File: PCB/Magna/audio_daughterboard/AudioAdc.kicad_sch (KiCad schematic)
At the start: 22 parts, among them J201 PSG01550, U201 WM8782SEDS

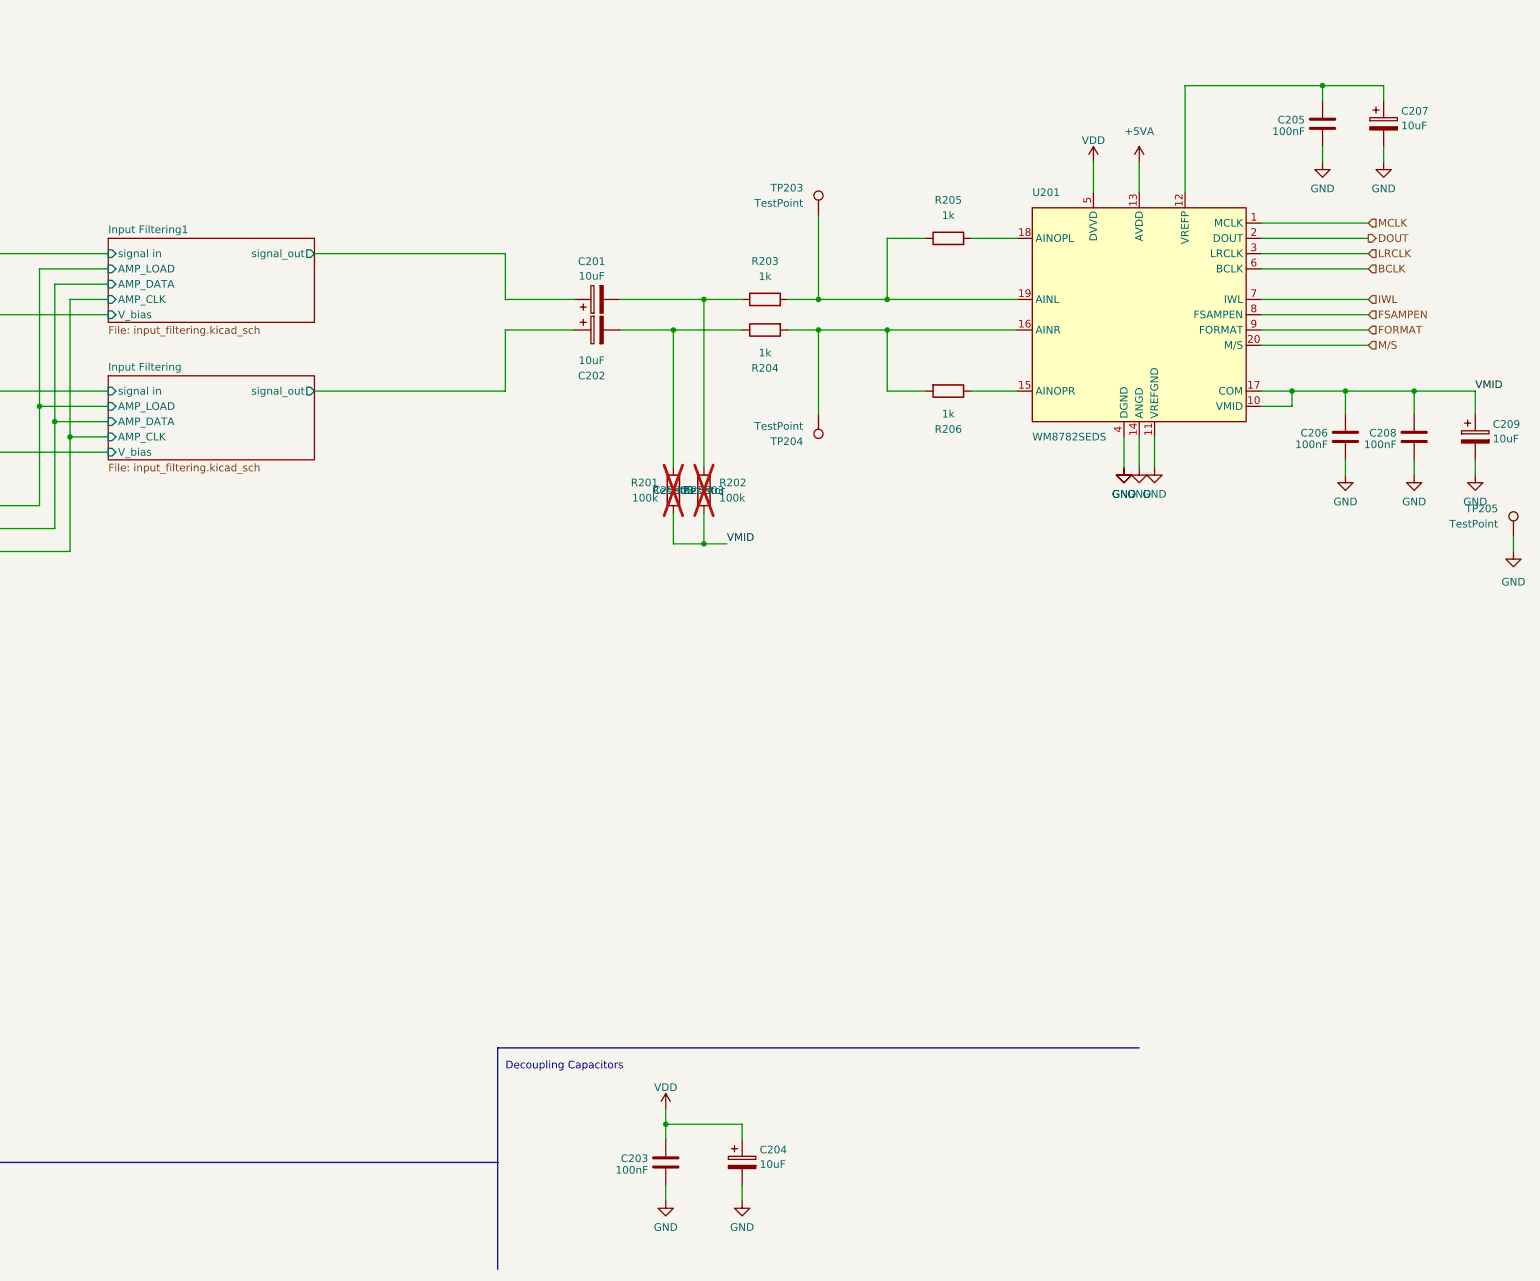
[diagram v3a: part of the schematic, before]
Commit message: Start layout and routing of Audio Daugherboard
Also a lot of small changes to everything that became apperant
when the audio daughterboard was designed. Such as the Headphone
PCB, which is now separate from the rest of the audio.
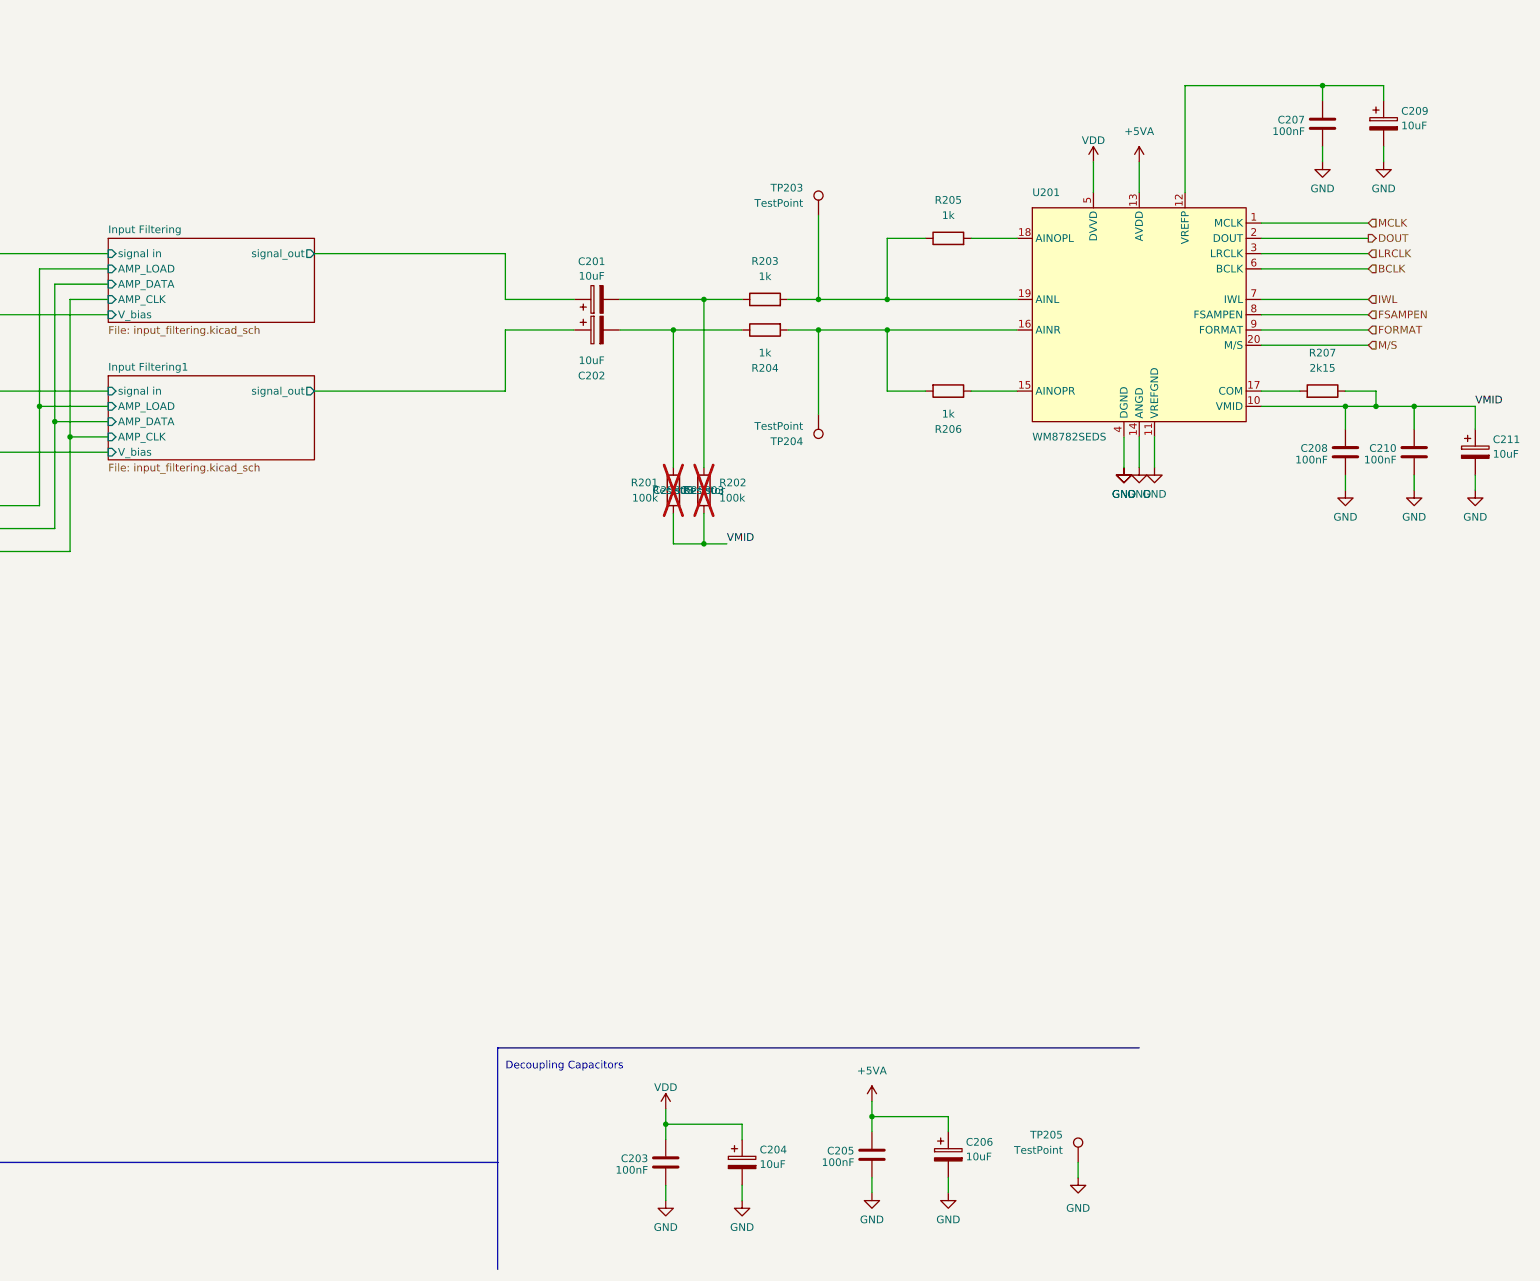
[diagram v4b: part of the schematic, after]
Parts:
- added C205: 100nF, Capacitor_SMD:C_0603_1608Metric, symbol Device:C
- added C206: 10uF, Capacitor_SMD:CP_Elec_4x5.8, symbol Device:C_Polarized
- added R207: 2k15, Resistor_SMD:R_0603_1608Metric, symbol Device:R
- renumbered C205 to C207, C206 to C208, C207 to C209, C208 to C210, C209 to C211
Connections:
- net +5VA: now also C205.1, C206.1
- net GND: now also C205.2, C206.2
- net Input Filtering/signal in: now also J201.1 (IN1), TP201.1; no longer J201.2 (IN2), TP202.1
- net Input Filtering/signal_out: now also C201.1; no longer C202.1
- net Input Filtering1/signal in: now also J201.2 (IN2), TP202.1; no longer J201.1 (IN1), TP201.1
- net Input Filtering1/signal_out: now also C202.1; no longer C201.1
- net VMID: now also R207.1; no longer U201.17 (COM)
- new net: R207.2, U201.17 (COM)
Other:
- moved on the sheet: C208, C210, C211, TP205

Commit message: Finished first round of routing for the Audio Daughterboard
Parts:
- removed C201, C202, C204, C206, C209, C211: 10uF, Capacitor_SMD:CP_Elec_4x5.8, symbol Device:C_Polarized
- removed R203, R204, R205, R206: 1k, Resistor_SMD:R_0603_1608Metric, symbol Device:R
- removed R207: 2k15, Resistor_SMD:R_0603_1608Metric, symbol Device:R
- removed TP203, TP204: TestPoint, TestPoint:TestPoint_Keystone_5005-5009_Compact, symbol Connector:TestPoint
- removed U201: WM8782SEDS, Package_SO:SSOP-20_5.3x7.2mm_P0.65mm, symbol Skrooter_symbols:WM8782SEDS
- added C201, C206, C211: 4.7uF, Capacitor_SMD:C_1206_3216Metric, symbol Device:C
- added C202, C204, C209: 100nF, Capacitor_SMD:C_0603_1608Metric, symbol Device:C
- added C212, C213: 10uF, Capacitor_SMD:CP_Elec_4x5.8, symbol Device:C_Polarized
- added TP203, TP204, TP205, TP206: TestPoint, TestPoint:TestPoint_Pad_1.0x1.0mm, symbol Connector:TestPoint_Alt
- added U201: NE5532, Package_SO:SOIC-8_3.9x4.9mm_P1.27mm, symbol Amplifier_Operational:NE5532
- added U202: CS5361, Package_SO:SOIC-24W_7.5x15.4mm_P1.27mm, symbol Audio:CS5361
- C207, C210: value 100nF -> 4.7uF; footprint Capacitor_SMD:C_0603_1608Metric -> Capacitor_SMD:C_1206_3216Metric; LCSC C14663 -> C29823; Votlage (none) -> 25V
- R201, R202: value 100k -> 10k; LCSC C25803 -> C95204; now fitted; now in the parts list
- renumbered TP205 to TP207
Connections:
- net +5VA: now also C201.1, C202.1, C213.1, U202.19 (VA); no longer C205.1
- net BCLK: now also U202.4 (SCLK)
- net DOUT: now also U202.9 (SDOUT)
- net GND: now also R201.2, C201.2, C202.2, C204.2, C206.2, C209.2, C211.2, C212.2, C213.2, U201.4 (V-), U202.18 (GND), U202.23 (REFGND), U202.7 (GND)
- net Input Filtering/signal in: now also J201.2 (IN2), TP202.1; no longer J201.1 (IN1), TP201.1
- net Input Filtering1/signal in: now also J201.1 (IN1), TP201.1; no longer J201.2 (IN2), TP202.1
- net LRCLK: now also U202.3 (LRCK)
- net MCLK: now also U202.5 (MCLK)
- net VDD: now also C208.1, C210.1, R202.1, C206.1, C212.1, U202.6 (VD), U202.8 (VL)
- net VQ: now reaches C207.1
- net VQ: now also C204.1, U202.22 (VQ)
- net ADC_RST: now reaches R201.1
- net ADC_RST: now also U202.1 (~{RST})
- removed net VMID: C208.1, C210.1, R201.2, R202.2
- new net: C209.1, C211.1, U202.24 (FILT+)
- new net ADC_HPF: U202.11 (~{HPF})
- new net ADC_I2S/LJ: U202.12 (I2S/~{LJ})
- new net ADC_M0: U202.14 (M1)
- new net ADC_M1: U202.13 (M0)
- new net ADC_MDIV: U202.10 (MDIV)
- new net ADC_M/S: U202.2 (M/~{S})
- new net ADC_OVFL: R202.2, U202.15 (~{OVFL})
- new net Input Filtering/INV+: U201.3 (+)
- new net Input Filtering/INV-: U201.2 (-)
- new net Input Filtering/INV_OUT: U201.1
- new net Input Filtering/signal_out+: TP205.1, U202.21 (AINR+)
- new net Input Filtering/signal_out-: TP206.1, U202.20 (AINR-)
- new net Input Filtering1/INV+: U201.5 (+)
- new net Input Filtering1/INV-: U201.6 (-)
- new net Input Filtering1/INV_OUT: U201.7
- new net Input Filtering1/signal_out+: TP203.1, U202.16 (AINL+)
- new net Input Filtering1/signal_out-: TP204.1, U202.17 (AINL-)
- new net VAA: C205.1, U201.8 (V+)
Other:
- sheet Input Filtering ports: added INV+, INV-, INV_OUT, VQ, signal_out+, signal_out-; removed signal_out
- sheet Input Filtering1 ports: added INV+, INV-, INV_OUT, VQ, signal_out+, signal_out-; removed signal_out
- moved on the sheet: J201, TP201, TP202, TP207

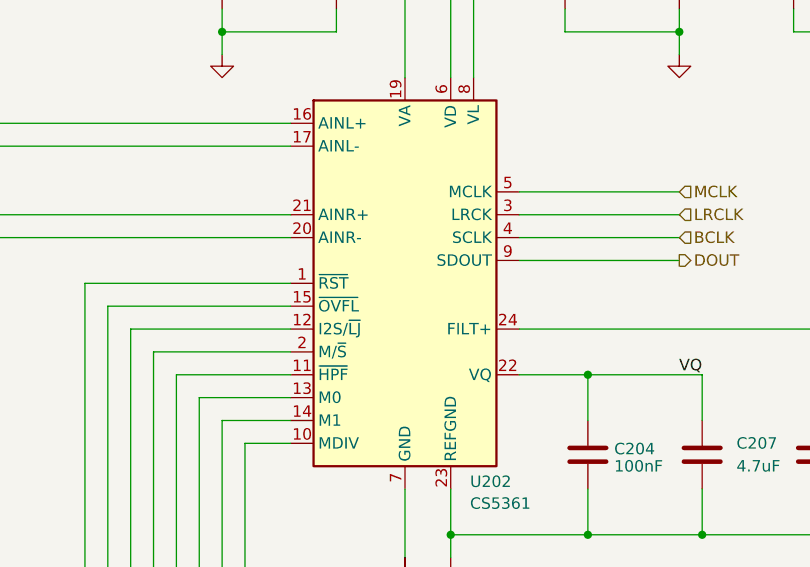
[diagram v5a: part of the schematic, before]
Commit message: Fix board alignments and mounting holes
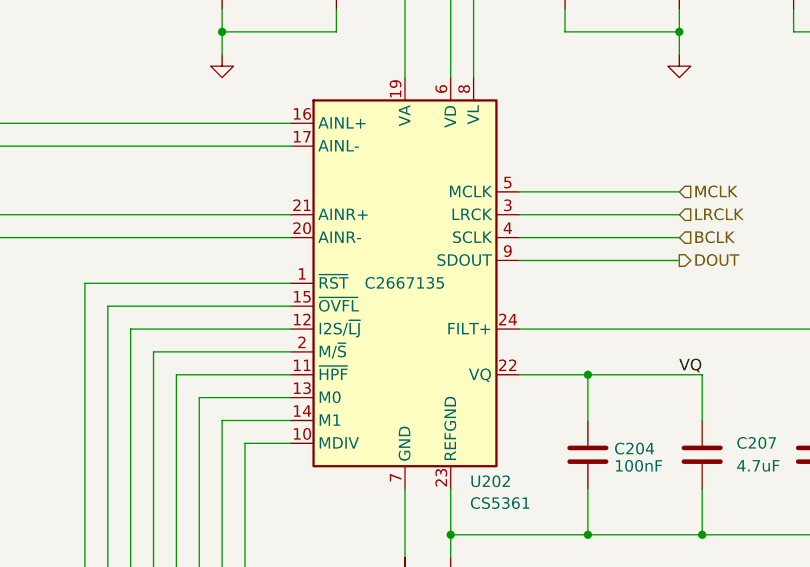
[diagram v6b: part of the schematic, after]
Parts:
- C201, C202, C203, C204, C205, C206, C207, C208, C209, C210, C211, C212, C213, U201: now in the parts list
- TP203, TP204, TP205, TP206: now left out of the parts list
- U202: LCSC (none) -> C2667135
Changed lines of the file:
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@@
 		(unit 1)
 		(exclude_from_sim no)
-		(in_bom no)
+		(in_bom yes)
 		(on_board yes)
 		(dnp no)
@@
 		(unit 1)
 		(exclude_from_sim no)
-		(in_bom no)
+		(in_bom yes)
 		(on_board yes)
 		(dnp no)
@@
 		(unit 1)
 		(exclude_from_sim no)
-		(in_bom no)
+		(in_bom yes)
 		(on_board yes)
 		(dnp no)
@@
 		(unit 1)
 		(exclude_from_sim no)
-		(in_bom no)
+		(in_bom yes)
 		(on_board yes)
 		(dnp no)
@@
 		(unit 1)
 		(exclude_from_sim no)
-		(in_bom no)
+		(in_bom yes)
 		(on_board yes)
 		(dnp no)
@@
 		(unit 1)
 		(exclude_from_sim no)
-		(in_bom no)
+		(in_bom yes)
 		(on_board yes)
 		(dnp no)
@@
 		(unit 1)
 		(exclude_from_sim no)
-		(in_bom no)
+		(in_bom yes)
 		(on_board yes)
 		(dnp no)
@@
 			)
 		)
+		(property "LCSC" "C2667135"
+			(at 294.64 101.6 0)
+			(effects
+				(font
+					(size 1.27 1.27)
+				)
+			)
+		)
 		(pin "4"
 		)
@@
 		(unit 2)
 		(exclude_from_sim no)
-		(in_bom no)
+		(in_bom yes)
 		(on_board yes)
 		(dnp no)
@@
 		(unit 1)
 		(exclude_from_sim no)
-		(in_bom no)
+		(in_bom yes)
 		(on_board yes)
 		(dnp no)
@@
 		(unit 1)
 		(exclude_from_sim no)
-		(in_bom no)
+		(in_bom yes)
 		(on_board yes)
 		(dnp no)
@@
 		(unit 3)
 		(exclude_from_sim no)
-		(in_bom no)
+		(in_bom yes)
 		(on_board yes)
 		(dnp no)
@@
 		(unit 1)
 		(exclude_from_sim no)
-		(in_bom no)
+		(in_bom yes)
 		(on_board yes)
 		(dnp no)
@@
 		(unit 1)
 		(exclude_from_sim no)
-		(in_bom yes)
+		(in_bom no)
 		(on_board yes)
 		(dnp no)
@@
 		(unit 1)
 		(exclude_from_sim no)
-		(in_bom no)
+		(in_bom yes)
 		(on_board yes)
 		(dnp no)
@@
 		(unit 1)
 		(exclude_from_sim no)
-		(in_bom yes)
+		(in_bom no)
 		(on_board yes)
 		(dnp no)
@@
 		(unit 1)
 		(exclude_from_sim no)
-		(in_bom no)
+		(in_bom yes)
 		(on_board yes)
 		(dnp no)
@@
 		(unit 1)
 		(exclude_from_sim no)
-		(in_bom no)
+		(in_bom yes)
 		(on_board yes)
 		(dnp no)
@@
 		(unit 1)
 		(exclude_from_sim no)
-		(in_bom yes)
+		(in_bom no)
 		(on_board yes)
 		(dnp no)
@@
 		(unit 1)
 		(exclude_from_sim no)
-		(in_bom yes)
+		(in_bom no)
 		(on_board yes)
 		(dnp no)
@@
 		(unit 1)
 		(exclude_from_sim no)
-		(in_bom no)
+		(in_bom yes)
 		(on_board yes)
 		(dnp no)
